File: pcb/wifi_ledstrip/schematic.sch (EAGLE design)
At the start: 1 part, among them IC1 STM32F10XCXT6

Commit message: main parts added
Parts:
- added HEARTBEAT, LED7, LED8, L_12V, L_3V3, L_5V, L_RX, L_TX: (no value), led:LEDSML1206
- added LED_STRIP_12V, LED_STRIP_GND, LED_STRIP_SIGNAL: (no value), SparkFun-Connectors:CONN_03SCREW
- added POWER: (no value), SparkFun-Connectors:CONN_025MM
- added PROGRAMMER: (no value), SparkFun-Connectors:CONN_03POLAR
- added SW_3, SW_4, SW_RESET, WIFI_RECONNECT: TACTILE_SWITCH_SIDETACTILE_SWITCH_SIDE, mylibrary:TACTILE_SWITCH_SIDETACTILE_SWITCH_SIDE
- added U$1, U$2, U$3: SN74LV1T34, mylibrary:SN74LV1T34
- added WIFI_MODUL: ESP01, esp8266modules:ESP01
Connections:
- new net GND: U$1.GND, U$2.GND, U$3.GND
- new net LED_STRIP_SIGNAL_1: U$3.LOGIC_IN
- new net LED_STRIP_SIGNAL_2: U$1.LOGIC_IN
- new net LED_STRIP_SIGNAL_3: U$2.LOGIC_IN
- new net N$1: LED_STRIP_SIGNAL.3, U$2.LOGIC_OUT
- new net N$2: LED_STRIP_SIGNAL.2, U$1.LOGIC_OUT
- new net N$3: LED_STRIP_SIGNAL.1, U$3.LOGIC_OUT
- new net VCC: U$1.VCC, U$2.VCC, U$3.VCC
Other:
- moved on the sheet: IC1PORTD/OSC

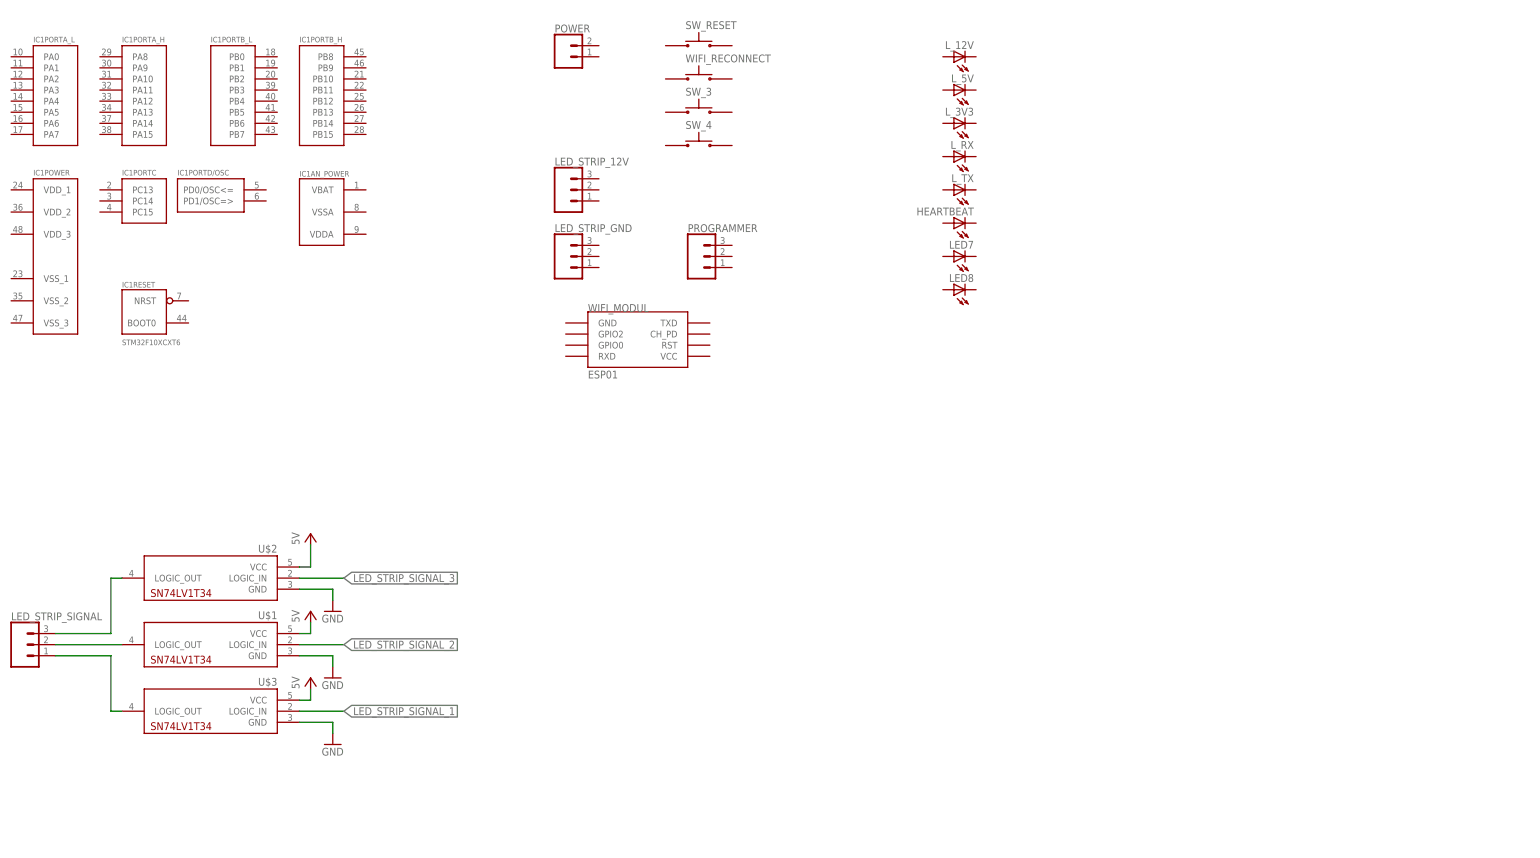
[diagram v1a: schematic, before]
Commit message: mikrocontroller capacitances, boot pins, reset button added
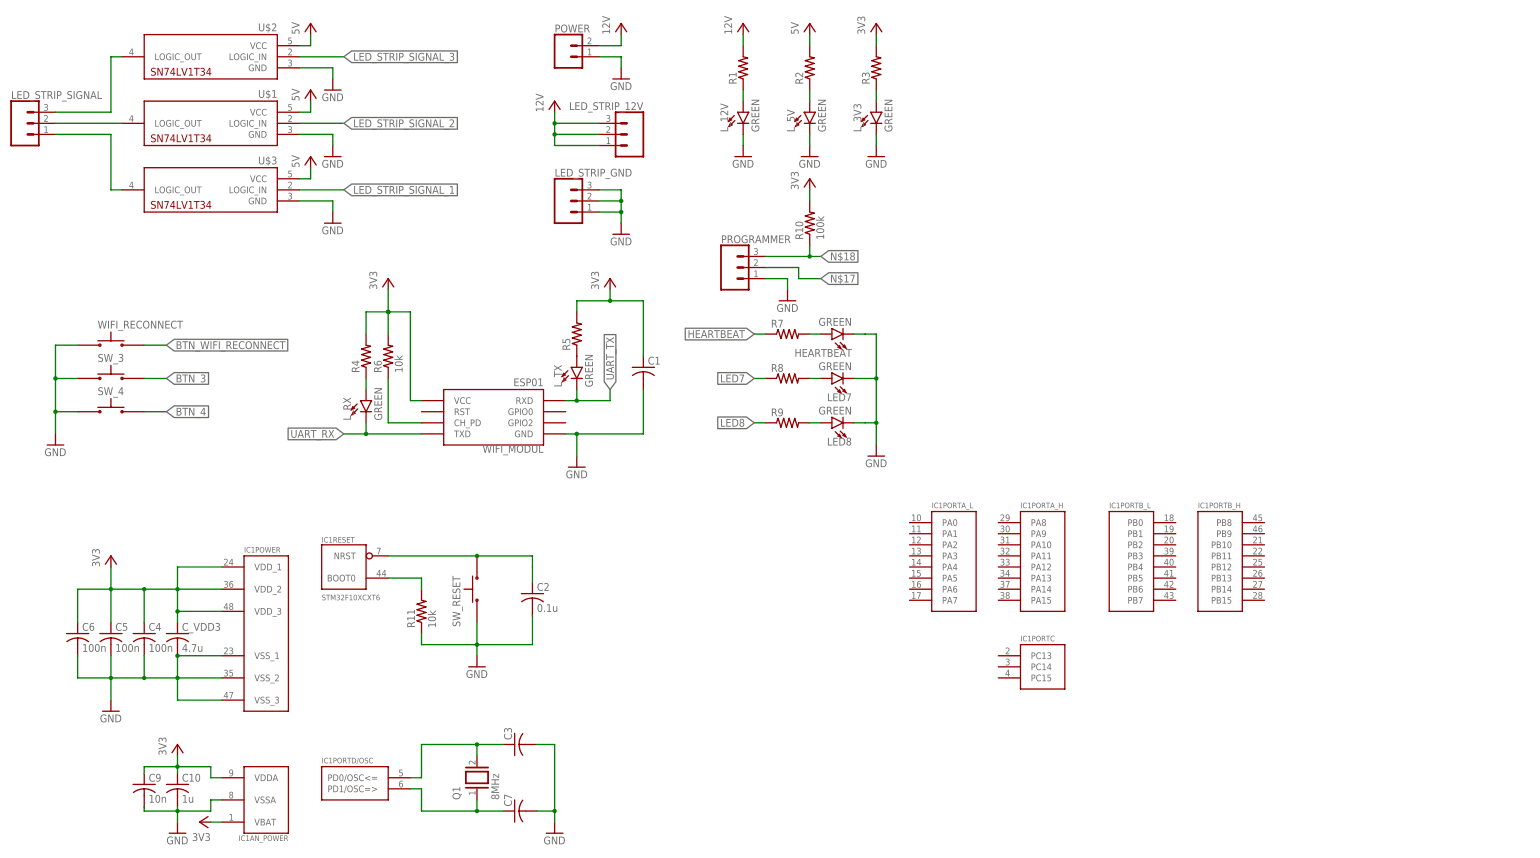
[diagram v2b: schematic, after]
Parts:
- added C1, C3, C7: (no value), rcl:C-USC1206
- added C10: 1u, rcl:C-USC1206
- added C2: 0.1u, rcl:C-USC1206
- added C4, C5, C6: 100n, rcl:C-USC1206
- added C9: 10n, rcl:C-USC1206
- added C_VDD3: 4.7u, rcl:C-USC1206
- added Q1: 8MHz, special:XTAL/S
- added R1, R2, R3, R4, R5, R7, R8, R9: (no value), rcl:R-US_R1206
- added R10: 100k, rcl:R-US_R1206
- added R11, R6: 10k, rcl:R-US_R1206
- HEARTBEAT, LED7, LED8, L_12V, L_3V3, L_5V, L_RX, L_TX: value (none) -> GREEN; device led:LEDSML1206 -> SparkFun-LED:LED-GREEN1206
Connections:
- new net BTN_3: SW_3.P$4
- new net BTN_4: SW_4.P$4
- new net BTN_WIFI_RECONNECT: WIFI_RECONNECT.P$4
- new net HEARTBEAT: R7.1
- new net LED7: R8.1
- new net LED8: R9.1
- new net N$10: HEARTBEAT.A, R7.2
- new net N$11: LED7.A, R8.2
- new net N$12: LED8.A, R9.2
- new net N$13: C2.1, IC1RESET.NRST, SW_RESET.P$3
- new net N$14: C3.1, IC1PORTD/OSC.PD0/OSC<=, Q1.2
- new net N$15: C7.1, IC1PORTD/OSC.PD1/OSC=>, Q1.1
- new net N$16: IC1RESET.BOOT0, R11.2
- new net N$17: PROGRAMMER.2
- new net N$18: PROGRAMMER.3, R10.1
- new net N$4: L_12V.A, R1.1
- new net N$5: L_5V.A, R2.1
- new net N$6: L_3V3.A, R3.1
- new net N$7: L_RX.A, R4.1
- new net N$8: R6.1, WIFI_MODUL.CH_PD
- new net N$9: L_TX.A, R5.1
- new net UART_RX: L_RX.C, WIFI_MODUL.TXD
- new net UART_TX: L_TX.C, WIFI_MODUL.RXD
- net GND: now also C1.2, C10.2, C2.2, C3.2, C4.2, C5.2, C6.2, C7.2, C9.2, C_VDD3.2, HEARTBEAT.C, IC1AN_POWER.VSSA, IC1POWER.VSS_1, IC1POWER.VSS_2, IC1POWER.VSS_3, LED7.C, LED8.C, LED_STRIP_GND.1, LED_STRIP_GND.2, LED_STRIP_GND.3, L_12V.C, L_3V3.C, L_5V.C, POWER.1, PROGRAMMER.1, R11.1, SW_3.P$3, SW_4.P$3, SW_RESET.P$4, WIFI_MODUL.GND, WIFI_RECONNECT.P$3
- net VCC: now also C1.1, C10.1, C4.1, C5.1, C6.1, C9.1, C_VDD3.1, IC1AN_POWER.VBAT, IC1AN_POWER.VDDA, IC1POWER.VDD_1, IC1POWER.VDD_2, IC1POWER.VDD_3, LED_STRIP_12V.1, LED_STRIP_12V.2, LED_STRIP_12V.3, POWER.2, R1.2, R10.2, R2.2, R3.2, R4.2, R5.2, R6.2, WIFI_MODUL.VCC
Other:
- moved on the sheet: IC1AN_POWER, IC1PORTA_H, IC1PORTA_L, IC1PORTB_H, IC1PORTB_L, IC1PORTC, IC1PORTD/OSC, IC1POWER, IC1RESET, LED_STRIP_12V, LED_STRIP_GND, LED_STRIP_SIGNAL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
